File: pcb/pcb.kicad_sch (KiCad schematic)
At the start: 16 parts

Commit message: finished everything but usb power up
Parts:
- removed J?: Conn_01x04_MountingPin, symbol Connector_Generic_MountingPin:Conn_01x04_MountingPin
- added J?: Conn_01x05, symbol Connector_Generic:Conn_01x05
- added J?: Conn_01x04, symbol Connector_Generic:Conn_01x04
- added SW?: SW_SPDT, symbol Switch:SW_SPDT
- added SW?: SW_DIP_x01, symbol Switch:SW_DIP_x01
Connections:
- net +3V3 is gone; now on net +3.3VA: C?.1, C?.1, C?.1, C?.1, C?.1, C?.1, R?.2, R?.2, U?.1 (VBAT), U?.19 (VDD), U?.32 (VDD), U?.48 (VDD), U?.64 (VDD)
- net +3.3VA: now also J?.2 (Pin_2), SW?.2 (B)
- net GND: now also J?.1 (Pin_1), J?.3 (Pin_3), SW?.1
- net SCL: now reaches R?.1, R?.2
- net SCL: now also J?.3 (Pin_3)
- net SDA: now reaches R?.1, R?.2
- net SDA: now also J?.4 (Pin_4)
- net SWDIO: now reaches U?.46 (PA13)
- net SWDIO: now also J?.2 (Pin_2)
- net SWCLK: now reaches U?.49 (PA14)
- net SWCLK: now also J?.1 (Pin_1)
- net NRST: now reaches C?.1, U?.7 (NRST)
- net NRST: now also J?.5 (Pin_5), SW?.2
- new net: J?.4 (Pin_4), SW?.3 (C)
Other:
- note added: "ORDER ------ SWCLK SWDIO GND 3.3V RESET"

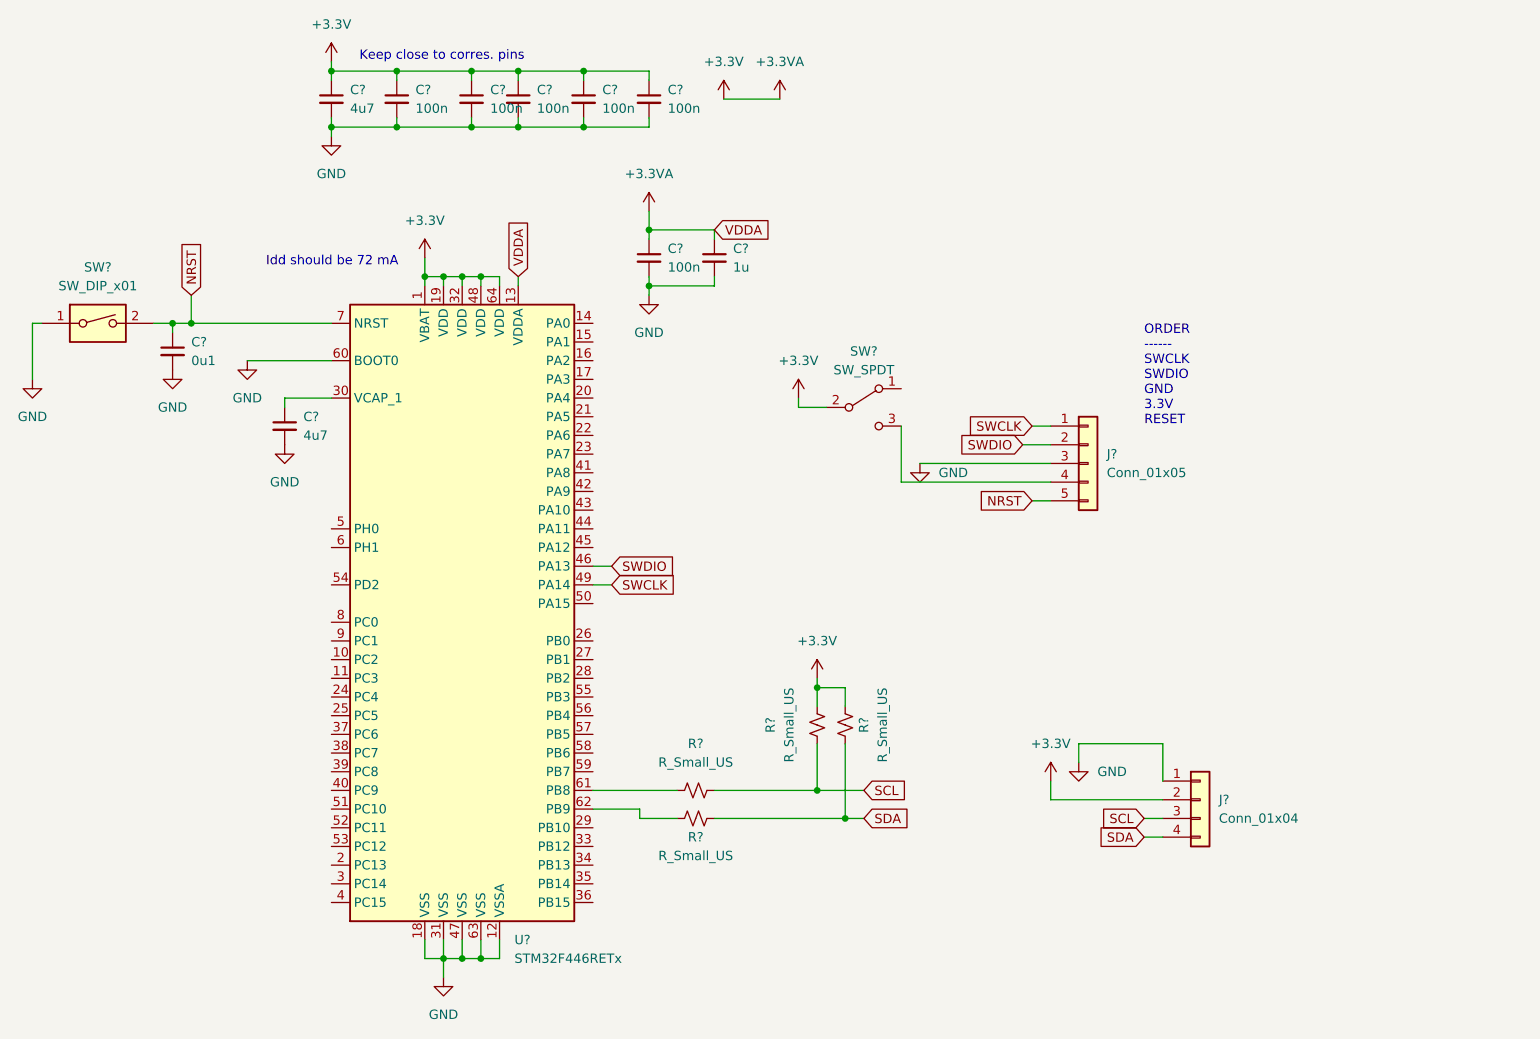
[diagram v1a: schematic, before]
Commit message: added buttons
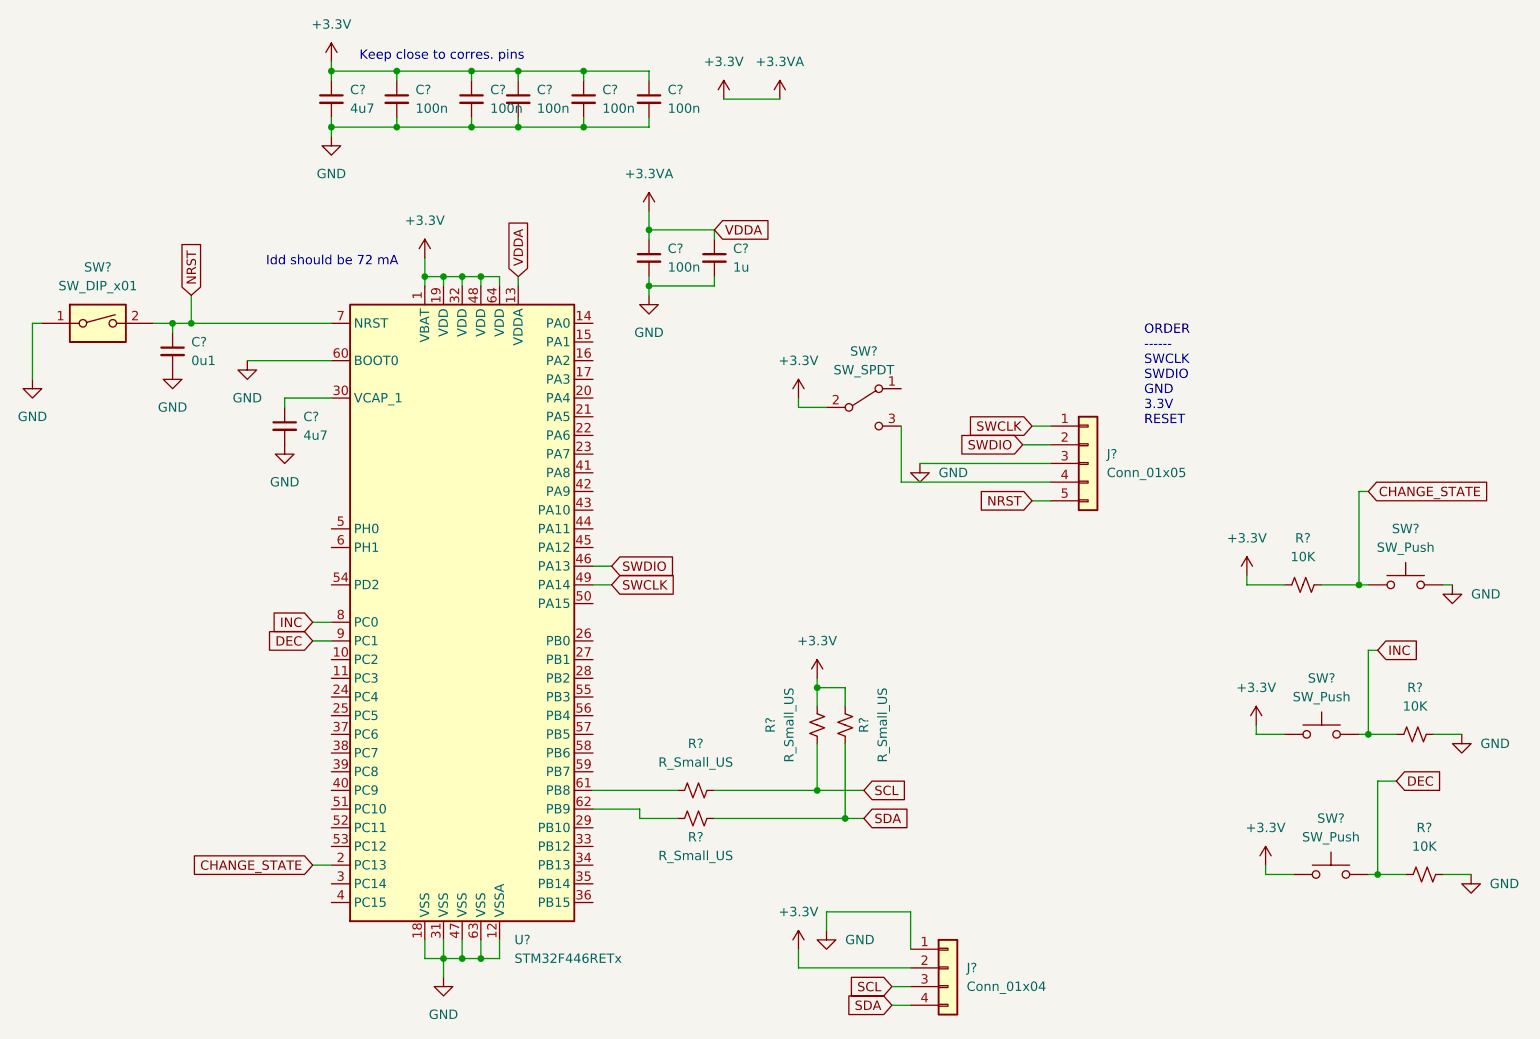
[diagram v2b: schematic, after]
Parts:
- added R? (x3): 10K, symbol Device:R_Small_US
- added SW? (x3): SW_Push, symbol Switch:SW_Push
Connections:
- net +3.3VA: now also R?.1, SW?.1, SW?.1
- net GND: now also R?.2, R?.2, SW?.2
- net CHANGE_STATE: now reaches U?.2 (PC13)
- net CHANGE_STATE: now also R?.2, SW?.1
- net INC: now reaches U?.8 (PC0)
- net INC: now also R?.1, SW?.2
- net DEC: now reaches U?.9 (PC1)
- net DEC: now also R?.1, SW?.2
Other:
- moved on the sheet: J?
